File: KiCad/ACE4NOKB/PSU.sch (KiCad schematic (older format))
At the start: 31 parts

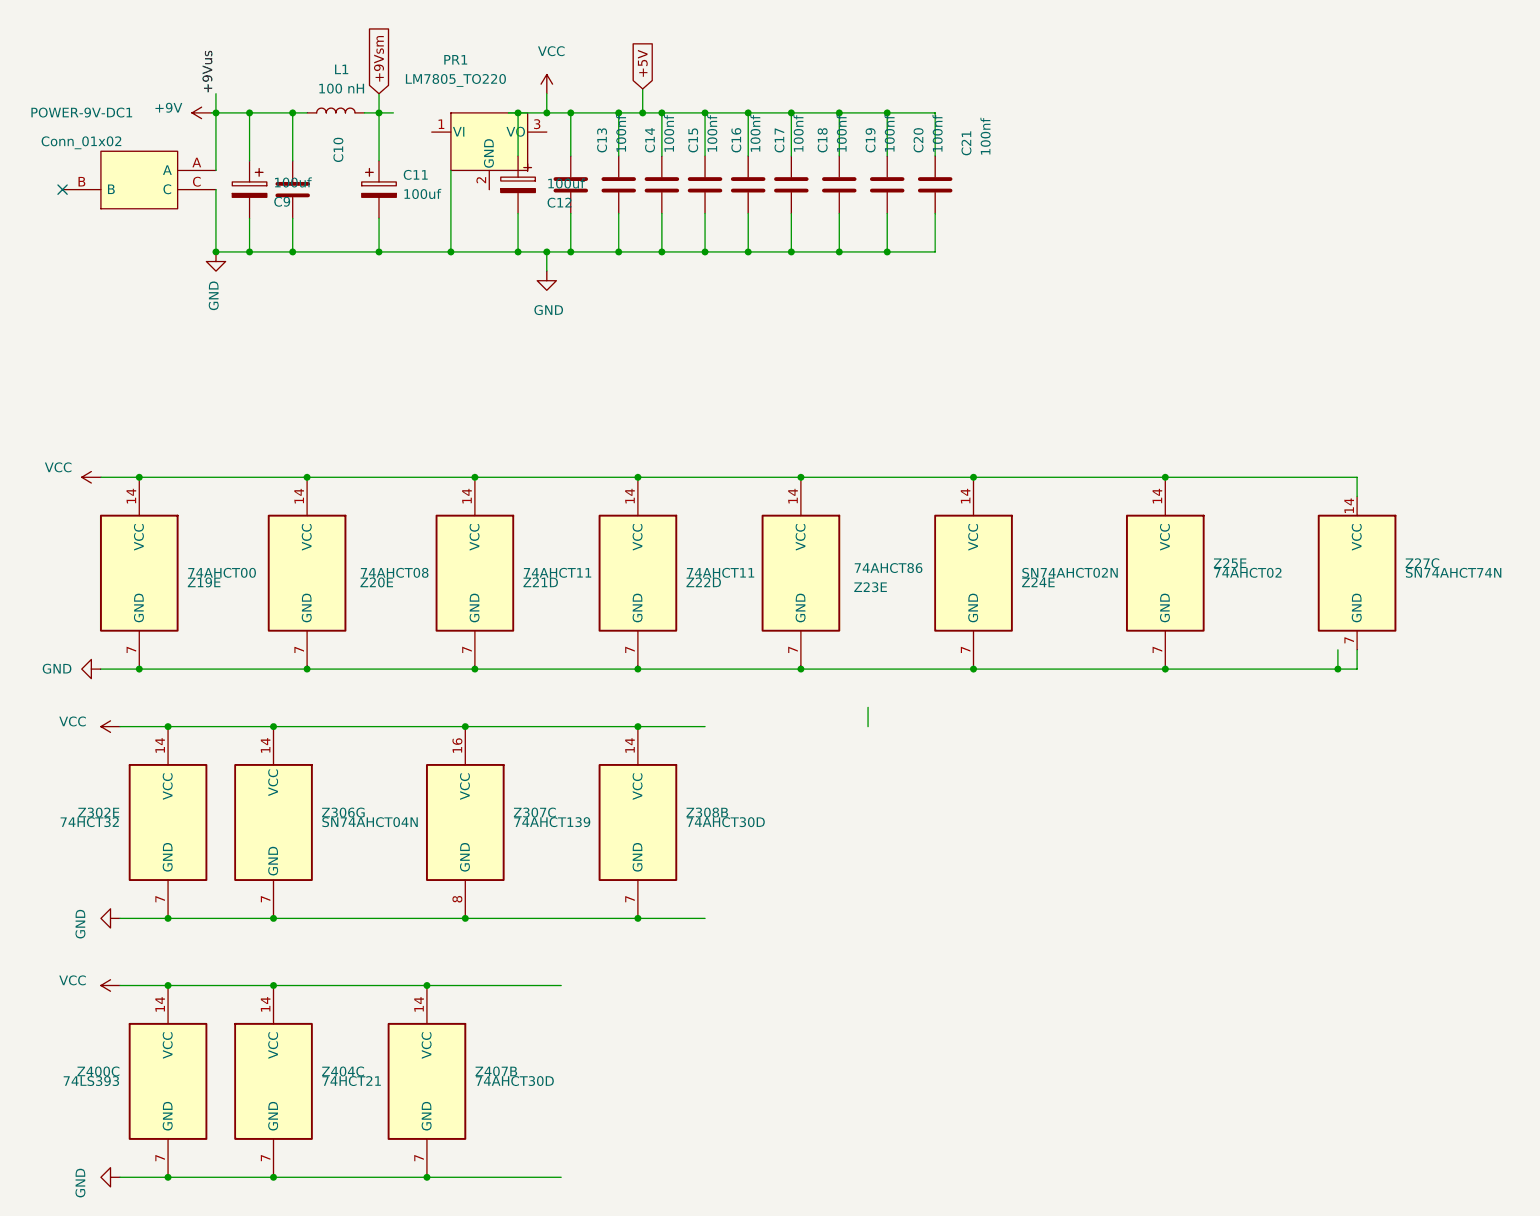
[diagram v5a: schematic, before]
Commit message: Update ACE3NOKB to reflect errors in Mem Decode. ACE5NOKB test SMT ideas. Added 180 & 380.
Signed-off-by: John Bradley <flypie@rocketmail.com>
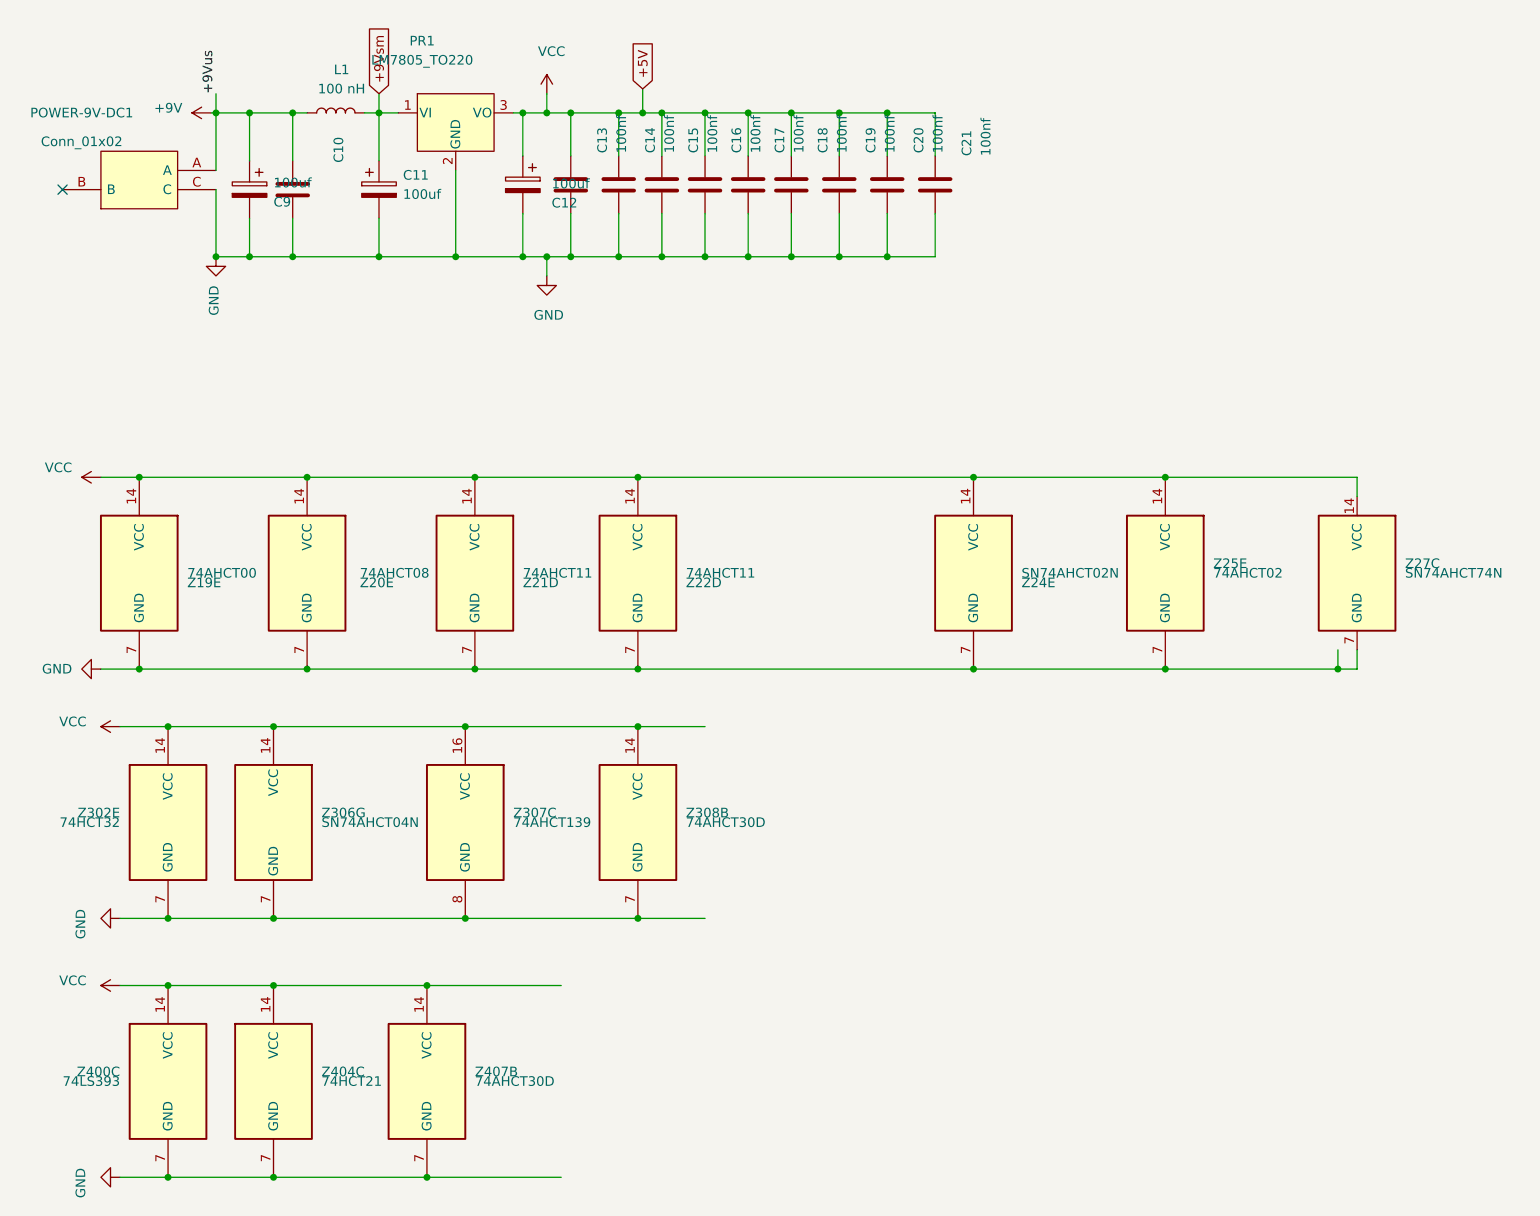
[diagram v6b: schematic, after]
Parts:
- removed Z23: 74AHCT86, Package_DIP:DIP-14_W7.62mm_Socket, symbol 74xx:74LS86
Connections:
- wire segments 106 -> 103
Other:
- moved on the sheet: C12, PR1
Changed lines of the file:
@@
 	0    -1   -1   0
-$EndComp
-$Comp
-L power:GND #~PWR0161
-U 1 1 731E2B46
-P 1400 1825
-F 0 "#~PWR0161" H 1400 1575 50  0001 C CNN
-F 1 "GND" V 1390 1675 50  0000 R CNN
-F 2 "" H 1400 1825 50  0001 C CNN
-F 3 "" H 1400 1825 50  0001 C CNN
-	1    1400 1825
-	1    0    0    -1
 $EndComp
 Text GLabel 2250 1000 1    50   Input ~ 0
@@
 	1    0    0    -1
 $EndComp
-$Comp
-L power:GND #~PWR0103
-U 1 1 5FF89C59
-P 3125 1925
-F 0 "#~PWR0103" H 3125 1675 50  0001 C CNN
-F 1 "GND" H 3135 1720 50  0000 C CNN
-F 2 "" H 3125 1925 50  0001 C CNN
-F 3 "" H 3125 1925 50  0001 C CNN
-	1    3125 1925
-	1    0    0    -1
-$EndComp
 Wire Wire Line
 	3125 1100 3250 1100
@@
 Connection ~ 4900 1100
 Wire Wire Line
-	3125 1925 3125 1825
-Wire Wire Line
-	3125 1825 3250 1825
-Wire Wire Line
 	4900 1100 5150 1100
-Connection ~ 4900 1825
-Wire Wire Line
-	4900 1825 5150 1825
-Connection ~ 4650 1825
-Wire Wire Line
-	4650 1825 4900 1825
-Connection ~ 4400 1825
-Wire Wire Line
-	4400 1825 4650 1825
-Connection ~ 4175 1825
-Wire Wire Line
-	4175 1825 4400 1825
-Connection ~ 3950 1825
-Wire Wire Line
-	3950 1825 4175 1825
-Connection ~ 3725 1825
-Wire Wire Line
-	3725 1825 3950 1825
-Connection ~ 3500 1825
-Wire Wire Line
-	3500 1825 3725 1825
-Connection ~ 3250 1825
-Wire Wire Line
-	3250 1825 3500 1825
-Connection ~ 3125 1825
-Wire Wire Line
-	2975 1625 2975 1825
-Connection ~ 2975 1825
-Wire Wire Line
-	2975 1825 3125 1825
-Wire Wire Line
-	2625 1400 2625 1825
-Wire Wire Line
-	2625 1825 2975 1825
-Wire Wire Line
-	2625 1825 2250 1825
-Connection ~ 2625 1825
-Wire Wire Line
-	2250 1650 2250 1825
-Connection ~ 2250 1825
-Wire Wire Line
-	2250 1825 1800 1825
-Connection ~ 1800 1825
-Wire Wire Line
-	1800 1825 1575 1825
-Wire Wire Line
-	1575 1650 1575 1825
-Connection ~ 1575 1825
-Wire Wire Line
-	1575 1825 1400 1825
 Wire Wire Line
 	2250 1000 2250 1100
@@
 Connection ~ 1575 1100
 Wire Wire Line
-	2975 1325 2975 1100
+	3000 1325 3000 1100
 Wire Wire Line
 	3125 1000 3125 1100
@@
 +5V
 Wire Wire Line
-	2975 1100 3125 1100
-Connection ~ 2975 1100
-Wire Wire Line
-	2925 1100 2975 1100
-Wire Wire Line
-	1800 1650 1800 1825
-Wire Wire Line
 	1800 1100 1800 1350
 Wire Wire Line
 	3250 1100 3250 1325
 Wire Wire Line
-	3250 1625 3250 1825
-Wire Wire Line
-	3500 1625 3500 1825
-Wire Wire Line
-	3725 1625 3725 1825
-Wire Wire Line
-	3950 1625 3950 1825
-Wire Wire Line
-	4175 1625 4175 1825
-Wire Wire Line
-	4650 1625 4650 1825
-Wire Wire Line
-	4900 1625 4900 1825
-Wire Wire Line
 	4900 1100 4900 1325
 Wire Wire Line
@@
 	4400 1100 4400 1325
 Wire Wire Line
-	4400 1625 4400 1825
-Wire Wire Line
-	5150 1625 5150 1825
-Wire Wire Line
 	5150 1100 5150 1325
 Wire Wire Line
 	3950 1100 3950 1325
-Wire Wire Line
-	4800 4300 4800 4200
 Wire Wire Line
 	7250 3900 7250 4000
@@
 Wire Wire Line
 	1400 1100 1575 1100
-Connection ~ 1400 1825
 $Comp
 L 74xx:74LS74 Z27
@@
 L Device:CP C12
 U 1 1 5F0A734F
-P 2975 1475
-F 0 "C12" H 2825 1380 50  0000 R CNN
-F 1 "100uf" H 2825 1480 50  0000 R CNN
-F 2 "Capacitor_THT:CP_Radial_D5.0mm_P2.00mm" H 3013 1325 50  0001 C CNN
-F 3 "" H 2975 1475 50  0001 C CNN
-	1    2975 1475
+P 3000 1475
+F 0 "C12" H 2850 1380 50  0000 R CNN
+F 1 "100uf" H 2850 1480 50  0000 R CNN
+F 2 "Capacitor_THT:CP_Radial_D5.0mm_P2.00mm" H 3038 1325 50  0001 C CNN
+F 3 "" H 3000 1475 50  0001 C CNN
+	1    3000 1475
 	-1   0    0    -1
 $EndComp
@@
 L Regulator_Linear:LM7805_TO220 PR1
 U 1 1 735D1281
-P 2625 1100
-F 0 "PR1" H 2650 1375 50  0000 C CNN
-F 1 "LM7805_TO220" H 2650 1275 50  0000 C CNN
-F 2 "Package_TO_SOT_THT:TO-220-3_Vertical" H 2625 1325 50  0001 C CIN
-F 3 "http://www.fairchildsemi.com/ds/LM/LM7805.pdf" H 2625 1050 50  0001 C CNN
-	1    2625 1100
-	1    0    0    -1
-$EndComp
-$Comp
-L 74xx:74LS86 Z23
-U 5 1 6A760723
-P 4450 3500
-F 0 "Z23" H 4175 3425 50  0000 R CNN
-F 1 "74AHCT86" H 4175 3525 50  0000 R CNN
-F 2 "Package_DIP:DIP-14_W7.62mm_Socket" H 4450 3500 50  0001 C CNN
-F 3 "74xx/74ls86.pdf" H 4450 3500 50  0001 C CNN
-	5    4450 3500
-	-1   0    0    -1
+P 2450 1000
+F 0 "PR1" H 2475 1275 50  0000 C CNN
+F 1 "LM7805_TO220" H 2475 1175 50  0000 C CNN
+F 2 "Package_TO_SOT_THT:TO-220-3_Vertical" H 2450 1225 50  0001 C CIN
+F 3 "http://www.fairchildsemi.com/ds/LM/LM7805.pdf" H 2450 950 50  0001 C CNN
+	1    2450 1000
+	1    0    0    -1
 $EndComp
 $Comp
@@
 Wire Wire Line
 	2250 1100 2250 1350
-Wire Wire Line
-	2250 1100 2325 1100
 $Comp
 L 74xx:74LS08 Z20
@@
 $EndComp
 Wire Wire Line
-	1400 1500 1400 1825
-Wire Wire Line
 	1400 1100 1400 1400
 Wire Wire Line
@@
 +9Vus
 $Comp
-L 74xx:74LS32 Z?
+L 74xx:74LS32 Z302
 U 5 1 601F2058
 P 1150 4800
-AR Path="/601F2058" Ref="Z?"  Part="5"
-AR Path="/5E5AD6B1/601F2058" Ref="Z302"  Part="5"
 F 0 "Z302" H 900 4850 50  0000 R CNN
 F 1 "74HCT32" H 900 4800 50  0000 R CNN
@@
 $EndComp
 $Comp
-L power:GND #~PWR?
+L power:GND #~PWR0125
 U 1 1 601F205E
 P 900 5300
-AR Path="/601F205E" Ref="#~PWR?"  Part="1"
-AR Path="/5E5AD6B1/601F205E" Ref="#~PWR0125"  Part="1"
 F 0 "#~PWR0125" H 900 5050 50  0001 C CNN
 F 1 "GND" H 930 5095 50  0000 C CNN
@@
 $EndComp
 $Comp
-L power:VCC #~PWR?
+L power:VCC #~PWR0127
 U 1 1 601F2064
 P 900 4300
-AR Path="/601F2064" Ref="#~PWR?"  Part="1"
-AR Path="/5E5AD6B1/601F2064" Ref="#~PWR0127"  Part="1"
 F 0 "#~PWR0127" H 900 4150 50  0001 C CNN
 F 1 "VCC" V 925 4475 50  0000 L CNN
@@
 $EndComp
 $Comp
-L power:GND #~PWR?
+L power:GND #~PWR0136
 U 1 1 60C7F34E
 P 900 6650
-AR Path="/60C7F34E" Ref="#~PWR?"  Part="1"
-AR Path="/5E5AD6B1/60C7F34E" Ref="#~PWR0136"  Part="1"
 F 0 "#~PWR0136" H 900 6400 50  0001 C CNN
 F 1 "GND" H 930 6445 50  0000 C CNN
@@
 $EndComp
 $Comp
-L power:VCC #~PWR?
+L power:VCC #~PWR0137
 U 1 1 60C7F358
 P 900 5650
-AR Path="/60C7F358" Ref="#~PWR?"  Part="1"
-AR Path="/5E5AD6B1/60C7F358" Ref="#~PWR0137"  Part="1"
 F 0 "#~PWR0137" H 900 5500 50  0001 C CNN
 F 1 "VCC" V 925 5825 50  0000 L CNN
@@
 Connection ~ 1150 5300
 $Comp
-L 74xx:74LS21 Z?
+L 74xx:74LS21 Z404
 U 3 1 60CAFE8F
 P 1700 6150
-AR Path="/60CAFE8F" Ref="Z?"  Part="3"
-AR Path="/5E5AD6B1/60CAFE8F" Ref="Z404"  Part="3"
 F 0 "Z404" H 1950 6200 50  0000 L CNN
 F 1 "74HCT21" H 1950 6150 50  0000 L CNN
@@
 Connection ~ 1150 5650
 $Comp
-L 74xx:74LS393 Z?
+L 74xx:74LS393 Z400
 U 3 1 60C7F376
 P 1150 6150
-AR Path="/60C7F376" Ref="Z?"  Part="3"
-AR Path="/5E5AD6B1/60C7F376" Ref="Z400"  Part="3"
 F 0 "Z400" H 900 6200 50  0000 R CNN
 F 1 "74LS393" H 900 6150 50  0000 R CNN
@@
 Wire Wire Line
 	2750 4000 3600 4000
-Wire Wire Line
-	3600 3000 4450 3000
-Wire Wire Line
-	3600 4000 4450 4000
-Connection ~ 4450 3000
-Connection ~ 4450 4000
 Connection ~ 5350 3000
 Connection ~ 5350 4000
-Wire Wire Line
-	4450 3000 5350 3000
-Wire Wire Line
-	4450 4000 5350 4000
 Wire Wire Line
 	7350 3000 7350 3100
@@
 Wire Wire Line
 	1700 5300 2700 5300
+Wire Wire Line
+	3600 3000 5350 3000
+Wire Wire Line
+	3600 4000 5350 4000
+Wire Wire Line
+	2350 1100 2250 1100
+Connection ~ 3000 1100
+Wire Wire Line
+	3000 1100 3125 1100
+Wire Wire Line
+	2950 1100 3000 1100
+Wire Wire Line
+	3000 1850 3125 1850
+Connection ~ 3000 1850
+Wire Wire Line
+	1400 1500 1400 1850
+Connection ~ 1400 1850
+Wire Wire Line
+	5150 1625 5150 1850
+Wire Wire Line
+	4400 1625 4400 1850
+Wire Wire Line
+	4900 1625 4900 1850
+Wire Wire Line
+	4650 1625 4650 1850
+Wire Wire Line
+	4175 1625 4175 1850
+Wire Wire Line
+	3950 1625 3950 1850
+Wire Wire Line
+	3725 1625 3725 1850
+Wire Wire Line
+	3500 1625 3500 1850
+Wire Wire Line
+	3250 1625 3250 1850
+Wire Wire Line
+	1800 1650 1800 1850
+Wire Wire Line
+	1575 1850 1400 1850
+Connection ~ 1575 1850
+Wire Wire Line
+	1575 1650 1575 1850
+Wire Wire Line
+	1800 1850 1575 1850
+Connection ~ 1800 1850
+Wire Wire Line
+	2250 1850 1800 1850
+Connection ~ 2250 1850
+Wire Wire Line
+	2250 1650 2250 1850
+Wire Wire Line
+	3000 1625 3000 1850
+Connection ~ 3125 1850
+Wire Wire Line
+	3250 1850 3500 1850
+Connection ~ 3250 1850
+Wire Wire Line
+	3500 1850 3725 1850
+Connection ~ 3500 1850
+Wire Wire Line
+	3725 1850 3950 1850
+Connection ~ 3725 1850
+Wire Wire Line
+	3950 1850 4175 1850
+Connection ~ 3950 1850
+Wire Wire Line
+	4175 1850 4400 1850
+Connection ~ 4175 1850
+Wire Wire Line
+	4400 1850 4650 1850
+Connection ~ 4400 1850
+Wire Wire Line
+	4650 1850 4900 1850
+Connection ~ 4650 1850
+Wire Wire Line
+	4900 1850 5150 1850
+Connection ~ 4900 1850
+Wire Wire Line
+	3125 1850 3250 1850
+Wire Wire Line
+	3125 1950 3125 1850
+$Comp
+L power:GND #~PWR0103
+U 1 1 5FF89C59
+P 3125 1950
+F 0 "#~PWR0103" H 3125 1700 50  0001 C CNN
+F 1 "GND" H 3135 1745 50  0000 C CNN
+F 2 "" H 3125 1950 50  0001 C CNN
+F 3 "" H 3125 1950 50  0001 C CNN
+	1    3125 1950
+	1    0    0    -1
+$EndComp
+$Comp
+L power:GND #~PWR0161
+U 1 1 731E2B46
+P 1400 1850
+F 0 "#~PWR0161" H 1400 1600 50  0001 C CNN
+F 1 "GND" V 1390 1700 50  0000 R CNN
+F 2 "" H 1400 1850 50  0001 C CNN
+F 3 "" H 1400 1850 50  0001 C CNN
+	1    1400 1850
+	1    0    0    -1
+$EndComp
+Wire Wire Line
+	2650 1400 2650 1850
+Wire Wire Line
+	2250 1850 2650 1850
+Connection ~ 2650 1850
+Wire Wire Line
+	2650 1850 3000 1850
 $EndSCHEMATC
